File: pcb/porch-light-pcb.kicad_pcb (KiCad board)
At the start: 2 copper layers, 0 parts

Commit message: footprint assignment
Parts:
- added C1: 220uF, Capacitor_THT:CP_Radial_D5.0mm_P2.50mm, F.Cu at (107.7, 82.6)
- added C2: 0.1uF, Capacitor_SMD:C_0603_1608Metric_Pad1.08x0.95mm_HandSolder, F.Cu at (114.4, 86.4)
- added J1: HA0300500000G, HA0300500000G:CONN_HA0300500000G_AMP, F.Cu at (91.8, 39.0)
- added J2: Conn_01x02, Connector_PinHeader_2.54mm:PinHeader_1x02_P2.54mm_Vertical, F.Cu at (148.5, 68.0)
- added K1: PRY2-3V-450-1A-EF, PRY2_3V_450_1A_EF:RELAY_PRY2-3V-450-1A-EF, F.Cu at (116.5, 43.2)
- added PS1: IRM-03-3.3, Converter_ACDC:Converter_ACDC_MeanWell_IRM-03-xx_THT, F.Cu at (91.8, 70.5)
- added Q1: PN2222A, Package_TO_SOT_THT:TO-92_Inline, F.Cu at (138.8, 69.8)
- added U1: ~, TENSTAR:TENSTAR_ESP32-C3-SUPERMINI, F.Cu at (147.8, 53.1)

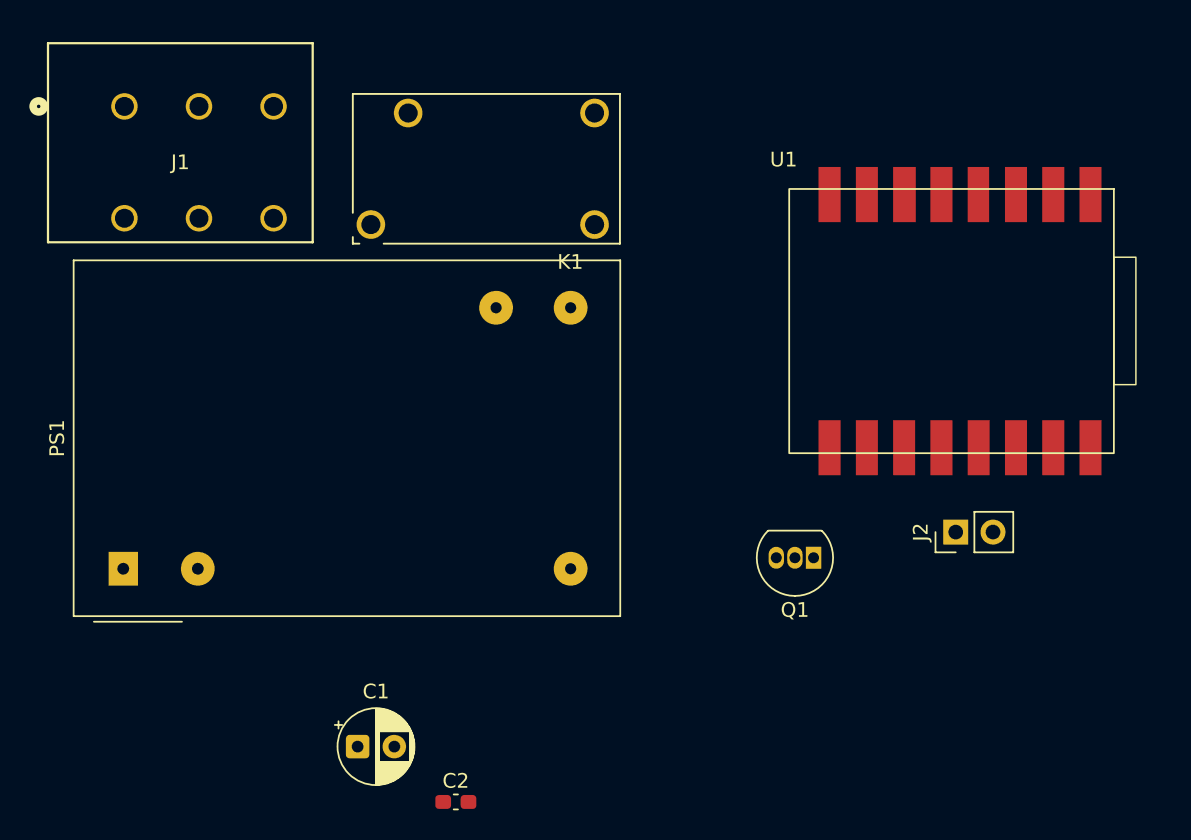
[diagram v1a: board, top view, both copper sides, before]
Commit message: intial board layout, chose some smaller parts
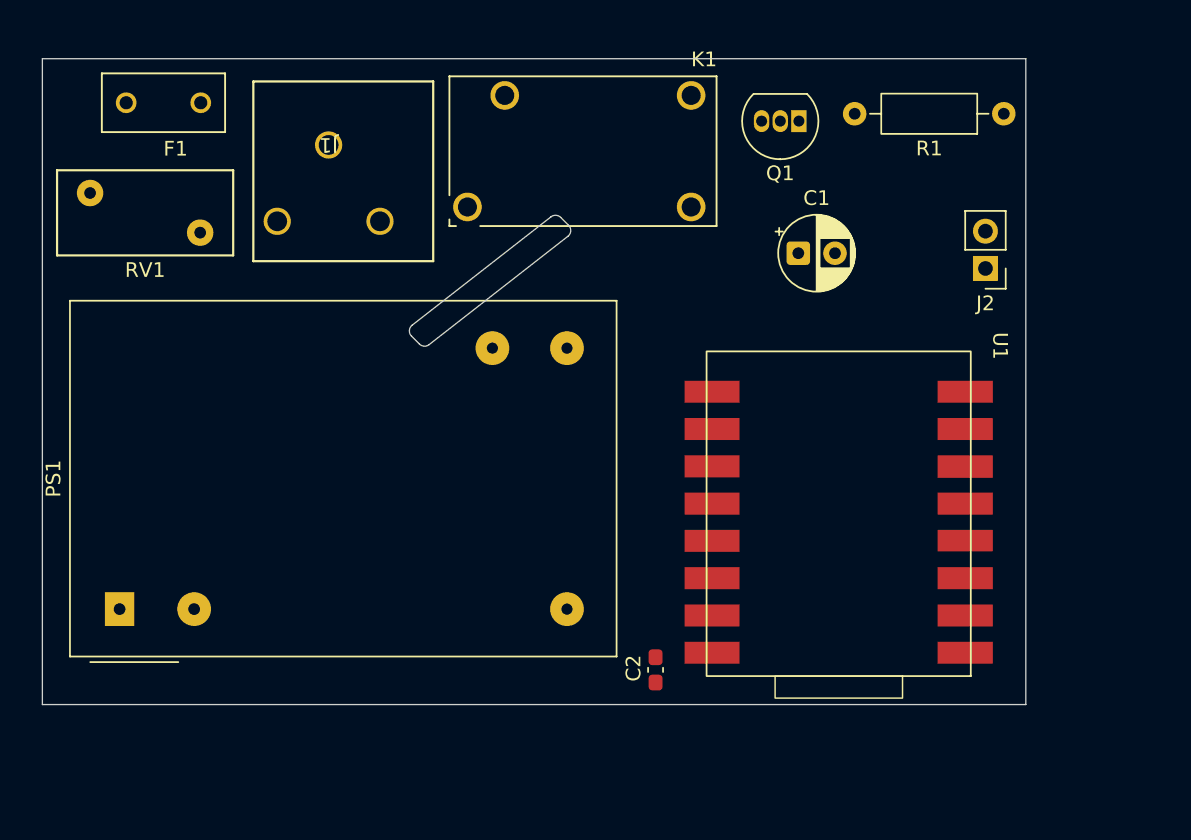
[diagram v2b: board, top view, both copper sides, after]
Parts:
- added F1: 0HAAL1000-02, 0HAAL1000_02:FUSRR508W60L840T400H810B, F.Cu at (94.5, 38.8)
- added R1: 270R, Resistor_THT:R_Axial_DIN0207_L6.3mm_D2.5mm_P10.16mm_Horizontal, F.Cu at (151.8, 39.5)
- added RV1: V150LA5P, Varistor:RV_Disc_D12mm_W5.8mm_P7.5mm, F.Cu at (89.5, 44.9)
- J1: value HA0300500000G -> 1-2834011-3; footprint HA0300500000G:CONN_HA0300500000G_AMP -> footprints:CONN_1-2834011-3_TEC
- moved C1 45.1 mm to (137.8, 49.0)
- moved Q1 29.8 mm to (137.8, 40.0)
- moved J1 19.1 mm to (109.3, 46.8), turned to 180 degrees
- moved J2 18.1 mm to (150.5, 50.0), turned to 180 degrees
- moved C2 16.3 mm to (128.0, 77.4), turned to -90 degrees
- moved U1 14.8 mm to (141.0, 66.3), turned to 180 degrees
- moved K1 6.69 mm to (123.1, 42.0)
- moved PS1 2.76 mm to (91.5, 73.2)
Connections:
- J1 pad 2: /AC_NEUTRAL -> /AC_LIVE
- J1 pad 3: /AC_LIVE -> Net-(J1-Pad3)
- K1 pad COM: Net-(J1-Pad5) -> Net-(J1-Pad3)
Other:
- board outline added: 67 x 44 mm

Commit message: fixed netclasses
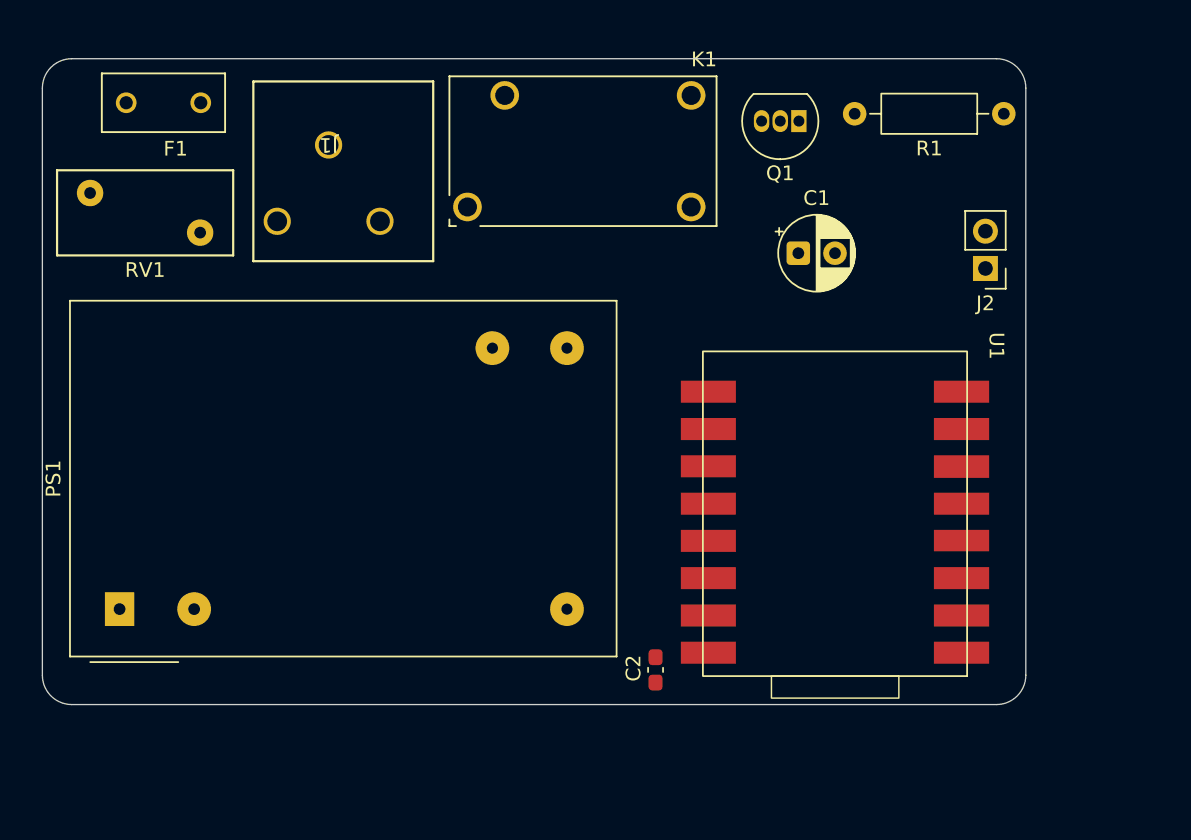
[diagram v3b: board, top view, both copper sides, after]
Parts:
- moved U1 0.25 mm to (140.8, 66.3)
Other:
- outline, holes or cut-outs redrawn
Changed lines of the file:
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@@
 	(footprint "TENSTAR:TENSTAR_ESP32-C3-SUPERMINI"
 		(layer "F.Cu")
-		(at 141 66.31 180)
+		(at 140.75 66.31 180)
 		(property "Reference" "U1"
 			(at -10.5 11 270)
@@
 			(polygon
 				(pts
-					(xy 144.5 59.19) (xy 136.5 59.19) (xy 136.5 54.69) (xy 144.5 54.69)
+					(xy 144.25 59.19) (xy 136.25 59.19) (xy 136.25 54.69) (xy 144.25 54.69)
 				)
 			)
@@
 		)
 	)
-	(gr_rect
-		(start 86.25 35.75)
-		(end 153.25 79.75)
-		(stroke
-			(width 0.05)
-			(type solid)
-		)
-		(fill no)
-		(layer "Edge.Cuts")
-	)
 	(gr_arc
-		(start 111.399819 54.649819)
-		(mid 111.254346 54.265631)
-		(end 111.445737 53.902108)
+		(start 86.25 37.75)
+		(mid 86.835786 36.335786)
+		(end 88.25 35.75)
 		(stroke
 			(width 0.05)
@@
 	)
 	(gr_line
-		(start 111.399819 54.649819)
-		(end 111.937359 55.187359)
+		(start 86.25 77.75)
+		(end 86.25 37.75)
 		(stroke
 			(width 0.05)
@@
 		(layer "Edge.Cuts")
 	)
-	(gr_arc
-		(start 112.598547 55.227963)
-		(mid 112.260261 55.332872)
-		(end 111.937359 55.187359)
+	(gr_line
+		(start 88.25 35.75)
+		(end 151.25 35.75)
 		(stroke
 			(width 0.05)
@@
 		(layer "Edge.Cuts")
 	)
-	(gr_line
-		(start 112.598547 55.227963)
-		(end 122.054263 47.847892)
+	(gr_arc
+		(start 88.25 79.75)
+		(mid 86.835786 79.164214)
+		(end 86.25 77.75)
 		(stroke
 			(width 0.05)
@@
 		(layer "Edge.Cuts")
 	)
-	(gr_line
-		(start 120.901453 46.522037)
-		(end 111.445737 53.902108)
+	(gr_arc
+		(start 151.25 35.75)
+		(mid 152.664214 36.335786)
+		(end 153.25 37.75)
 		(stroke
 			(width 0.05)
@@
 		(layer "Edge.Cuts")
 	)
-	(gr_arc
-		(start 120.901453 46.522037)
-		(mid 121.239736 46.417135)
-		(end 121.562641 46.562641)
+	(gr_line
+		(start 151.25 79.75)
+		(end 88.25 79.75)
 		(stroke
 			(width 0.05)
@@
 	)
 	(gr_line
-		(start 122.100181 47.100181)
-		(end 121.562641 46.562641)
+		(start 153.25 37.75)
+		(end 153.25 77.75)
 		(stroke
 			(width 0.05)
@@
 	)
 	(gr_arc
-		(start 122.100181 47.100181)
-		(mid 122.245654 47.484369)
-		(end 122.054263 47.847892)
+		(start 153.25 77.75)
+		(mid 152.664214 79.164214)
+		(end 151.25 79.75)
 		(stroke
 			(width 0.05)

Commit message: finished routing
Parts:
- moved R1 0.90 mm to (151.0, 40.0)
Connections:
- net Net-(J1-Pad3) renamed /AC_RELAY
- net Net-(PS1-AC/L) renamed /AC_FILTERED
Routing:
- net +3.3V: track 0.00 -> 56.3 mm
- net /AC_NEUTRAL: track 0.00 -> 40.4 mm
- net /AC_FILTERED: track 0.00 -> 36.5 mm
- net /RELAY_GPIO: track 0.00 -> 26.7 mm
- net /AC_LIVE: track 0.00 -> 23.7 mm
- net /BUTTON_GPIO: track 0.00 -> 23.0 mm
- net /AC_RELAY: track 0.00 -> 15.1 mm
- net GND: track 0.00 -> 7.60 mm
- net Net-(Q1-B): track 0.00 -> 6.87 mm
- net /RELAY_GND: track 0.00 -> 5.52 mm
- added copper zone on B.Cu, net GND
- added copper zone on F.Cu, net GND
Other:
- outline, holes or cut-outs redrawn

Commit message: updated gitignore
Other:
- board text added: "BTN_GPIO"
- board text added: "GND"
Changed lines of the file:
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@@
 		(at 123.08 42.05 180)
 		(property "Reference" "K1"
-			(at -8.25 6.25 0)
+			(at -6.67 -6.7 0)
 			(layer "F.SilkS")
 			(effects
@@
 		(layer "Edge.Cuts")
 	)
+	(gr_text "GND\n"
+		(at 149 48 0)
+		(layer "B.SilkS")
+		(effects
+			(font
+				(size 1 1)
+				(thickness 0.1)
+			)
+			(justify left bottom mirror)
+		)
+	)
+	(gr_text "BTN_GPIO"
+		(at 149 50.75 0)
+		(layer "B.SilkS")
+		(effects
+			(font
+				(size 1 1)
+				(thickness 0.1)
+			)
+			(justify left bottom mirror)
+		)
+	)
 	(segment

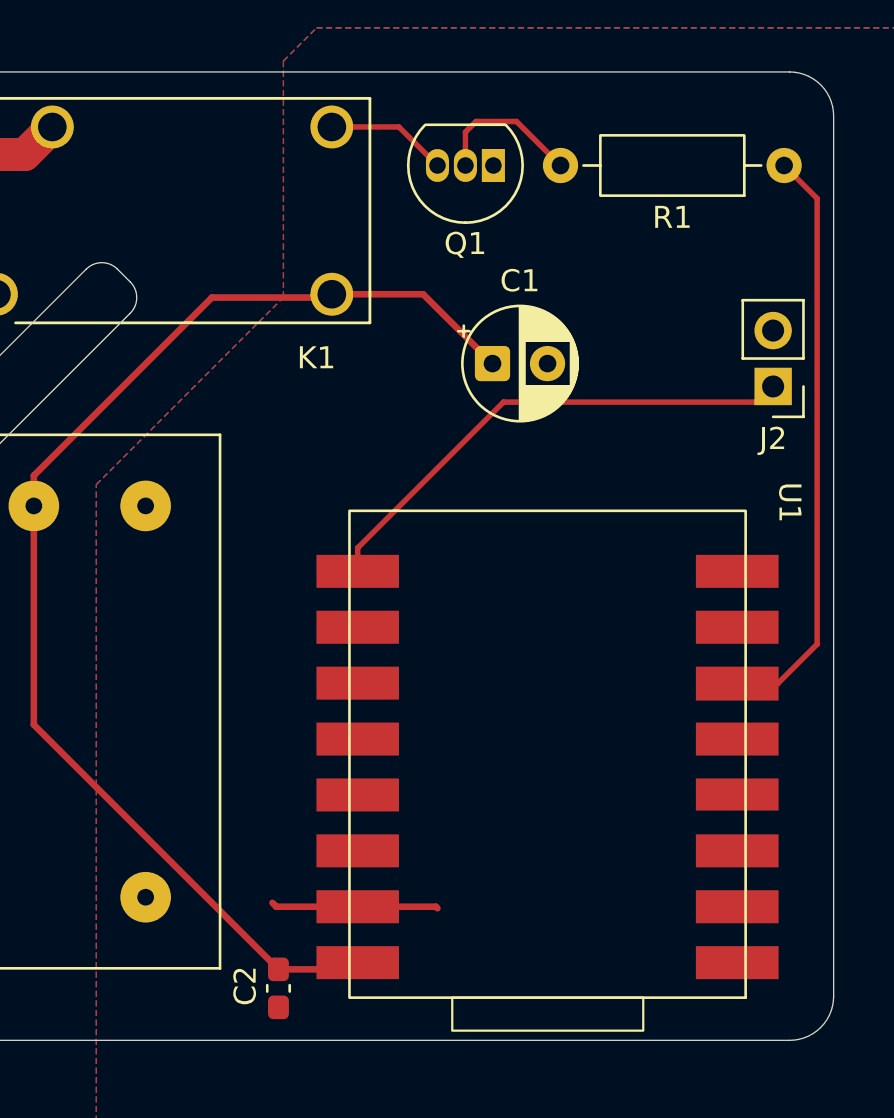
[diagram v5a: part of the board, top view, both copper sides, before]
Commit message: updated gitignore, add stiching vias
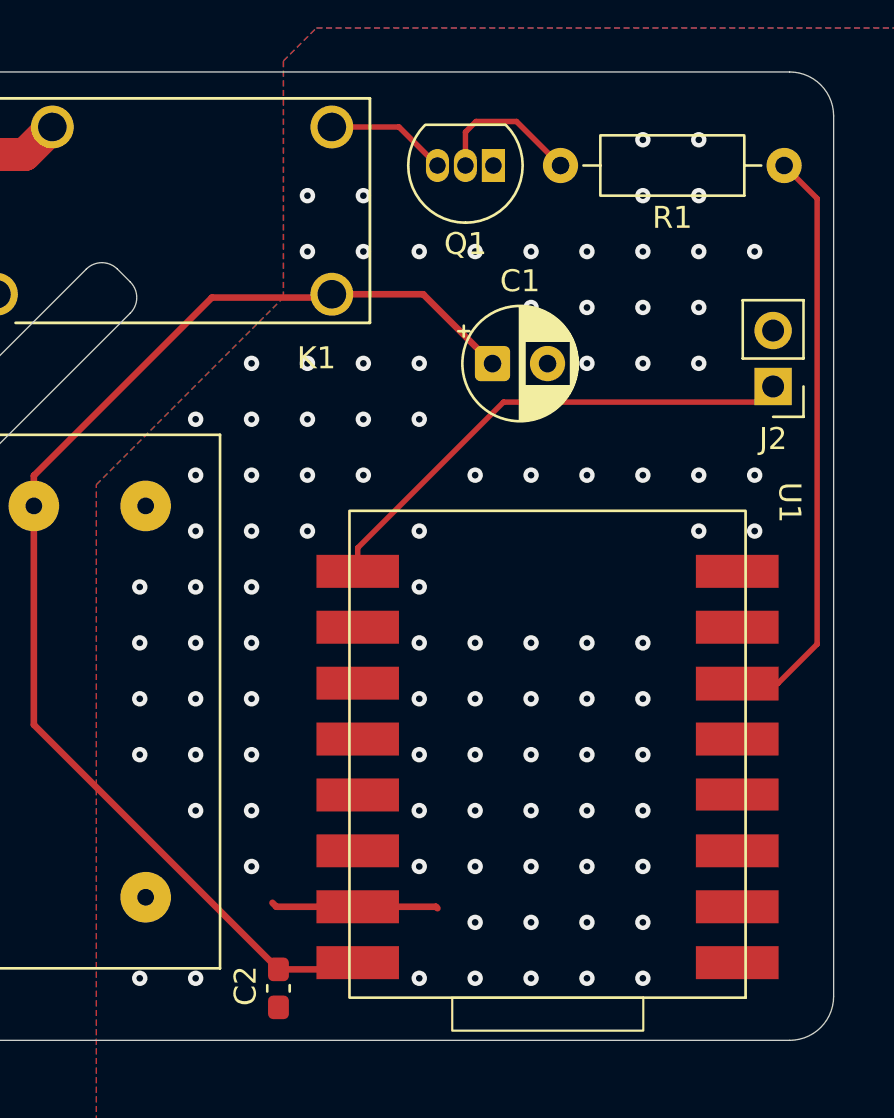
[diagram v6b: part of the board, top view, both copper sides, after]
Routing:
- net GND: vias 0 -> 99
